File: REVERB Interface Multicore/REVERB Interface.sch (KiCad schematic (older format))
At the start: 71 parts, among them J1 RPiZeroW, J2 Iridium, J3 APRS, J4 Antenna, J5 UPDI, M1 MountingHole_Pad, M2 MountingHole_Pad, M3 MountingHole_Pad, M4 MountingHole_Pad, M5 PiMount, M6 PiMount, M7 PiMount, M8 PiMount, U1 IMU, U2 MAX3232, U3 ATtiny1604-SS, U4 TXB0104D

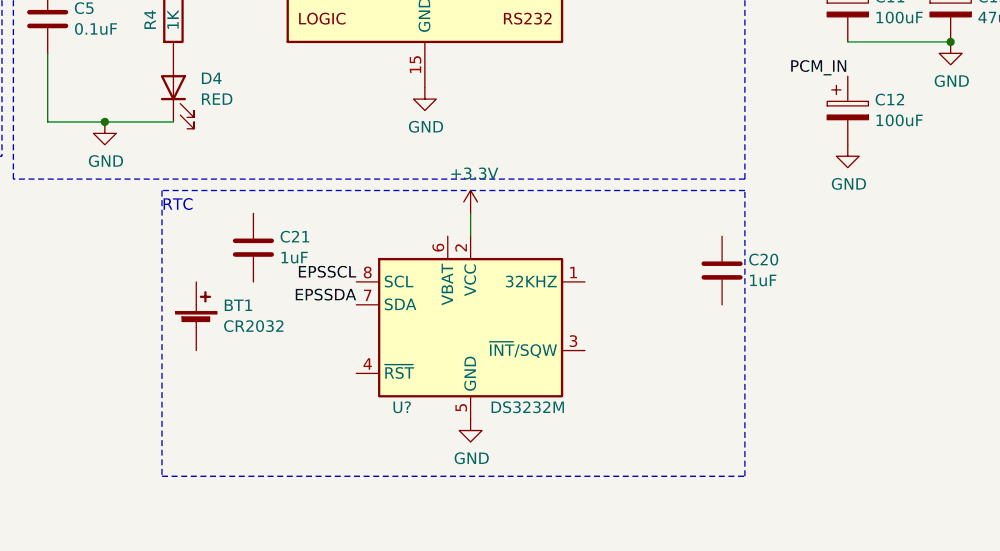
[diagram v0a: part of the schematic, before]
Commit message: add footprints, may need to use smaller battery
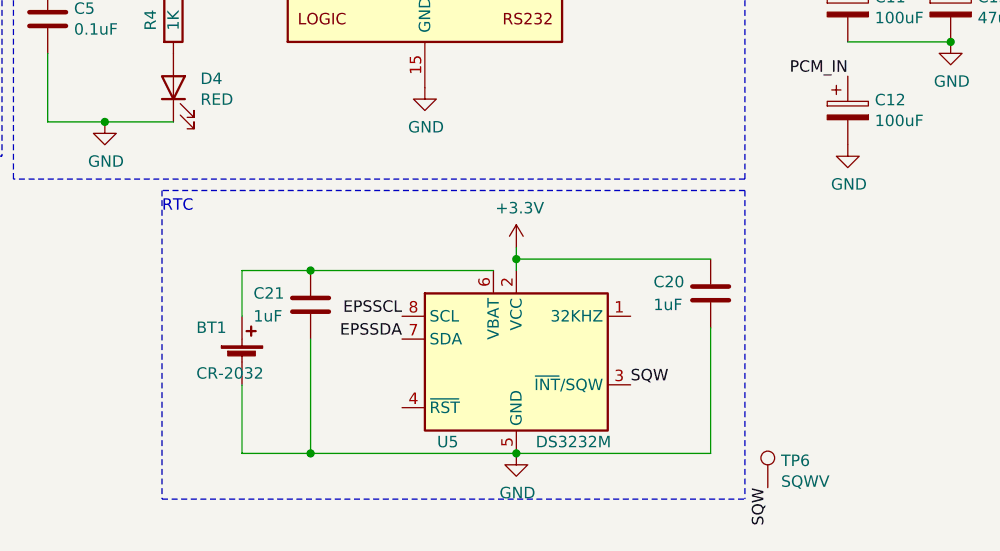
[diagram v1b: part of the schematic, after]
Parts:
- added TP6: SQWV, TestPoint:TestPoint_Pad_D2.0mm, symbol Connector:TestPoint
- BT1: value CR2032 -> CR-2032; footprint (none) -> REVERB Interface:CR2032-LINX-HLD-001-THM
- gave numbers to parts that had none: 1
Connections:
- net +3V3: now also C20.1
- net GND: now also BT1.2 (-), C20.2, C21.2
- net SQW: now reaches U5.3 (~INT~/SQW)
- net SQW: now also TP6.1
- net at U5.6 (VBAT): now also BT1.1 (+), C21.1
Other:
- moved on the sheet: BT1, C20, C21, U5
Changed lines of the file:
@@
 L Device:C C21
 U 1 1 61971DD0
-P 4750 7000
-F 0 "C21" H 4865 7046 50  0000 L CNN
-F 1 "1uF" H 4865 6955 50  0000 L CNN
-F 2 "Capacitor_SMD:C_0805_2012Metric_Pad1.18x1.45mm_HandSolder" H 4788 6850 50  0001 C CNN
-F 3 "~" H 4750 7000 50  0001 C CNN
-	1    4750 7000
+P 5000 7250
+F 0 "C21" H 4750 7300 50  0000 L CNN
+F 1 "1uF" H 4750 7200 50  0000 L CNN
+F 2 "Capacitor_SMD:C_0805_2012Metric_Pad1.18x1.45mm_HandSolder" H 5038 7100 50  0001 C CNN
+F 3 "~" H 5000 7250 50  0001 C CNN
+	1    5000 7250
 	1    0    0    -1
 $EndComp
@@
 L Device:C C20
 U 1 1 619749F1
-P 6800 7100
-F 0 "C20" H 6915 7146 50  0000 L CNN
-F 1 "1uF" H 6915 7055 50  0000 L CNN
-F 2 "Capacitor_SMD:C_0805_2012Metric_Pad1.18x1.45mm_HandSolder" H 6838 6950 50  0001 C CNN
-F 3 "~" H 6800 7100 50  0001 C CNN
-	1    6800 7100
+P 6750 7200
+F 0 "C20" H 6500 7250 50  0000 L CNN
+F 1 "1uF" H 6500 7150 50  0000 L CNN
+F 2 "Capacitor_SMD:C_0805_2012Metric_Pad1.18x1.45mm_HandSolder" H 6788 7050 50  0001 C CNN
+F 3 "~" H 6750 7200 50  0001 C CNN
+	1    6750 7200
 	1    0    0    -1
 $EndComp
-Text Label 5200 7150 2    50   ~ 0
+Text Label 5400 7300 2    50   ~ 0
 EPSSCL
-Text Label 5200 7250 2    50   ~ 0
+Text Label 5400 7400 2    50   ~ 0
 EPSSDA
 $Comp
@@
 RTC
 Wire Notes Line
-	4350 6750 4350 8000
-Wire Notes Line
-	4350 8000 6900 8000
-Wire Notes Line
-	6900 8000 6900 6750
+	4350 8100 6900 8100
 Wire Notes Line
 	6900 6750 4350 6750
 $Comp
-L power:GND #PWR?
+L power:GND #PWR0141
 U 1 1 61943473
-P 5700 7750
-F 0 "#PWR?" H 5700 7500 50  0001 C CNN
-F 1 "GND" H 5705 7577 50  0000 C CNN
-F 2 "" H 5700 7750 50  0001 C CNN
-F 3 "" H 5700 7750 50  0001 C CNN
-	1    5700 7750
+P 5900 7900
+F 0 "#PWR0141" H 5900 7650 50  0001 C CNN
+F 1 "GND" H 5905 7727 50  0000 C CNN
+F 2 "" H 5900 7900 50  0001 C CNN
+F 3 "" H 5900 7900 50  0001 C CNN
+	1    5900 7900
 	1    0    0    -1
 $EndComp
 $Comp
-L Timer_RTC:DS3232M U?
-U 1 1 61946450
-P 5700 7350
-F 0 "U?" H 5400 7000 50  0000 C CNN
-F 1 "DS3232M" H 5950 7000 50  0000 C CNN
-F 2 "Package_SO:SOIC-8_3.9x4.9mm_P1.27mm" H 5750 6850 50  0001 C CNN
-F 3 "http://datasheets.maximintegrated.com/en/ds/DS3232M.pdf" H 5970 7500 50  0001 C CNN
-	1    5700 7350
+L power:+3.3V #PWR0142
+U 1 1 61947E10
+P 5900 7000
+F 0 "#PWR0142" H 5900 6850 50  0001 C CNN
+F 1 "+3.3V" H 5915 7173 50  0000 C CNN
+F 2 "" H 5900 7000 50  0001 C CNN
+F 3 "" H 5900 7000 50  0001 C CNN
+	1    5900 7000
+	1    0    0    -1
+$EndComp
+Wire Wire Line
+	5900 7000 5900 7050
+Wire Wire Line
+	5800 7100 5000 7100
+Wire Wire Line
+	4700 7100 4700 7300
+Connection ~ 5000 7100
+Wire Wire Line
+	5000 7100 4700 7100
+Wire Wire Line
+	4700 7600 4700 7900
+Wire Wire Line
+	4700 7900 5000 7900
+Connection ~ 5900 7900
+Connection ~ 5000 7900
+Wire Wire Line
+	5000 7900 5900 7900
+Wire Wire Line
+	5000 7400 5000 7900
+Wire Wire Line
+	6750 7050 5900 7050
+Connection ~ 5900 7050
+Wire Wire Line
+	5900 7050 5900 7100
+Wire Wire Line
+	5900 7900 6750 7900
+Wire Wire Line
+	6750 7900 6750 7350
+Text Label 6400 7600 0    50   ~ 0
+SQW
+$Comp
+L Connector:TestPoint TP6
+U 1 1 61969E5D
+P 7000 8050
+F 0 "TP6" H 7058 8168 50  0000 L CNN
+F 1 "SQWV" H 7058 8077 50  0000 L CNN
+F 2 "TestPoint:TestPoint_Pad_D2.0mm" H 7200 8050 50  0001 C CNN
+F 3 "~" H 7200 8050 50  0001 C CNN
+	1    7000 8050
+	1    0    0    -1
+$EndComp
+Text Label 7000 8050 3    50   ~ 0
+SQW
+Wire Notes Line
+	4350 6750 4350 8100
+Wire Notes Line
+	6900 6750 6900 8100
+$Comp
+L Device:Battery_Cell BT1
+U 1 1 6194D163
+P 4700 7500
+F 0 "BT1" H 4500 7650 50  0000 L CNN
+F 1 "CR-2032" H 4500 7450 50  0000 L CNN
+F 2 "REVERB Interface:CR2032-LINX-HLD-001-THM" V 4700 7560 50  0001 C CNN
+F 3 "~" V 4700 7560 50  0001 C CNN
+	1    4700 7500
 	1    0    0    -1
 $EndComp
 $Comp
-L power:+3.3V #PWR?
-U 1 1 61947E10
-P 5700 6850
-F 0 "#PWR?" H 5700 6700 50  0001 C CNN
-F 1 "+3.3V" H 5715 7023 50  0000 C CNN
-F 2 "" H 5700 6850 50  0001 C CNN
-F 3 "" H 5700 6850 50  0001 C CNN
-	1    5700 6850
+L Timer_RTC:DS3232M U5
+U 1 1 61946450
+P 5900 7500
+F 0 "U5" H 5600 7150 50  0000 C CNN
+F 1 "DS3232M" H 6150 7150 50  0000 C CNN
+F 2 "Package_SO:SOIC-8_3.9x4.9mm_P1.27mm" H 5950 7000 50  0001 C CNN
+F 3 "http://datasheets.maximintegrated.com/en/ds/DS3232M.pdf" H 6170 7650 50  0001 C CNN
+	1    5900 7500
 	1    0    0    -1
 $EndComp
-Wire Wire Line
-	5700 6850 5700 6950
-$Comp
-L Device:Battery_Cell BT1
-U 1 1 6194D163
-P 4500 7350
-F 0 "BT1" H 4618 7446 50  0000 L CNN
-F 1 "CR2032" H 4618 7355 50  0000 L CNN
-F 2 "" V 4500 7410 50  0001 C CNN
-F 3 "~" V 4500 7410 50  0001 C CNN
-	1    4500 7350
-	1    0    0    -1
-$EndComp

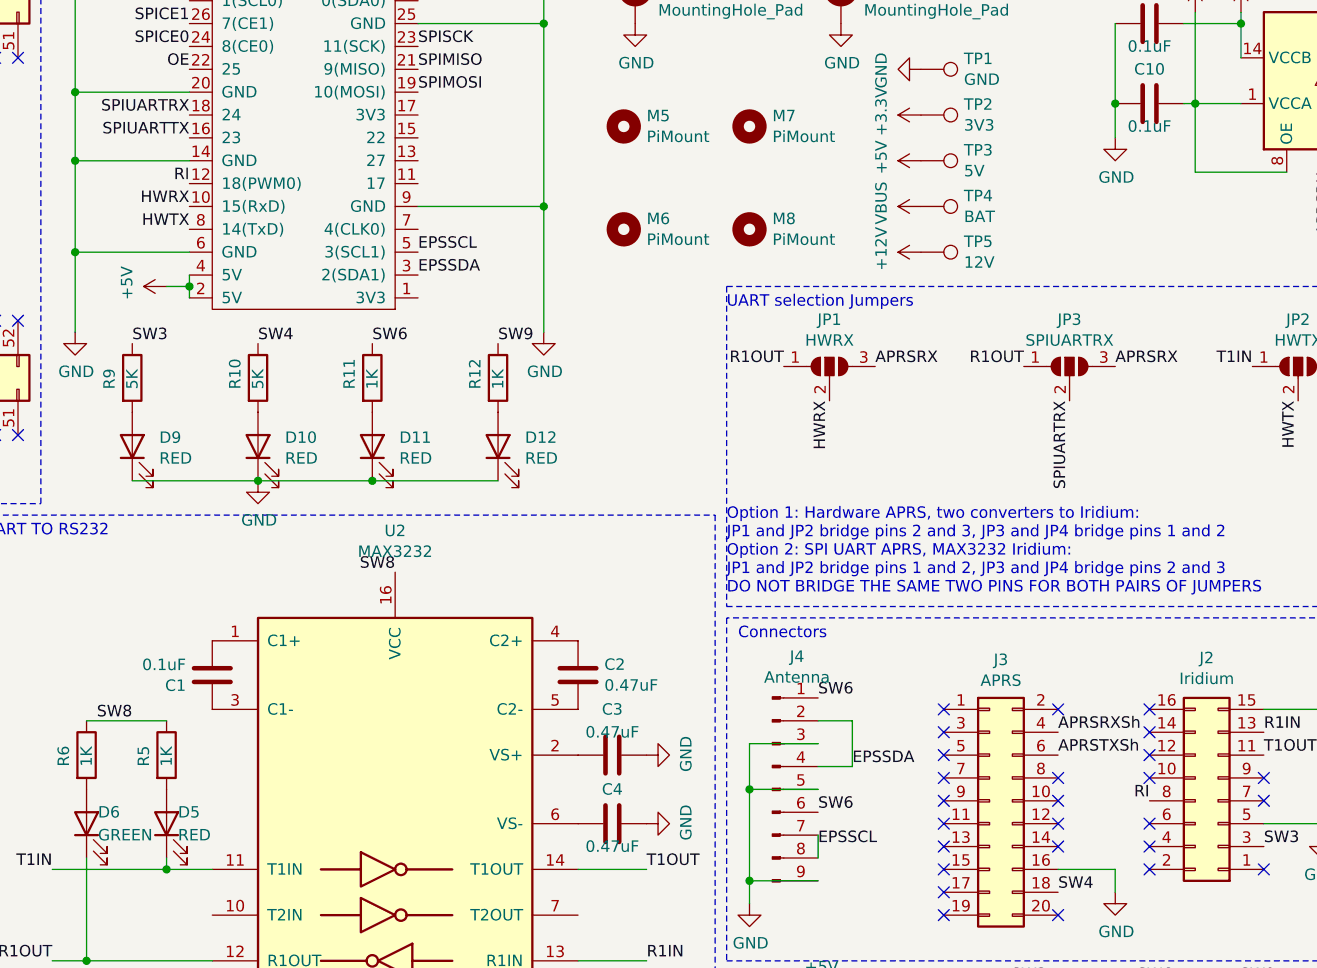
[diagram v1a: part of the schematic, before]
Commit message: Remove RI line
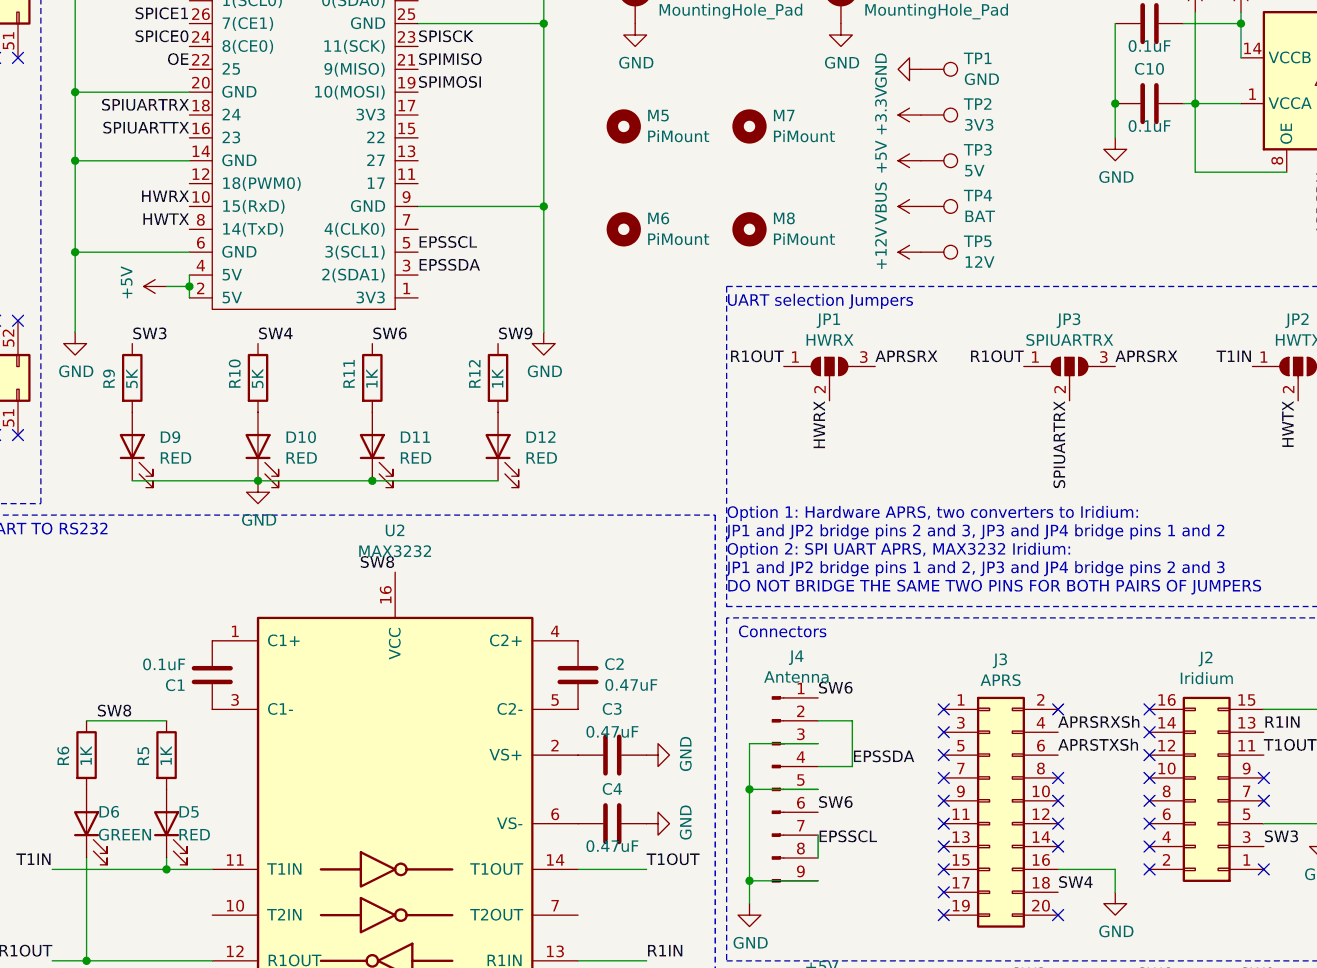
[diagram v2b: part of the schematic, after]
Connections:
- net RI: no longer names the net of J1.12 (18(PWM0))
- net RI: no longer J2.8 (Pin_8)
- no-connect marks 97 -> 98
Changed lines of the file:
@@
 	9550 4500 9300 4500
 Connection ~ 9550 5000
-Text Label 8800 4900 2    50   ~ 0
-RI
-Text Label 4600 2200 2    50   ~ 0
-RI
 $Comp
 L Device:C C21
@@
 	1    0    0    -1
 $EndComp
+NoConn ~ 8800 4900
 $EndSCHEMATC

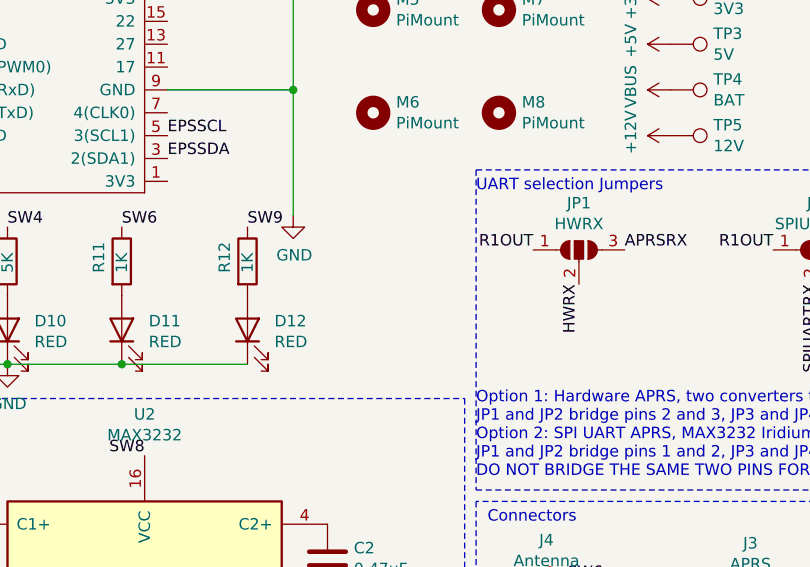
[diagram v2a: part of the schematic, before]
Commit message: add usb switch
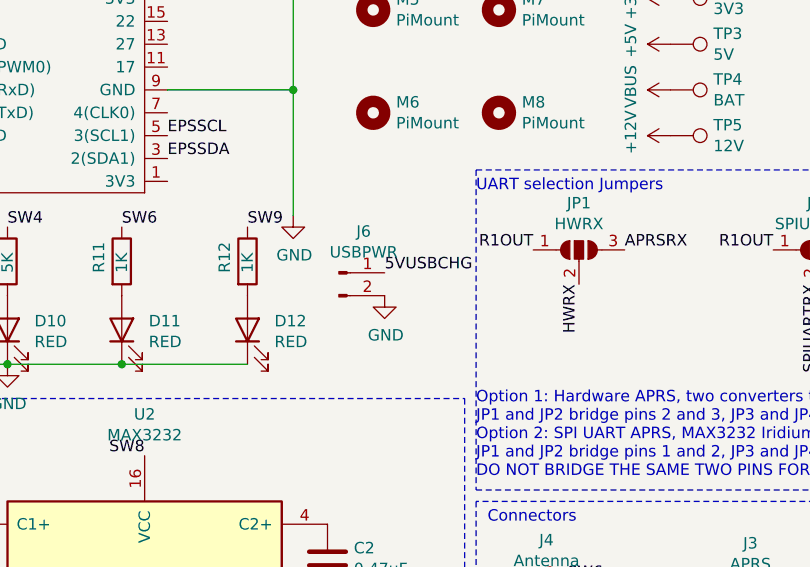
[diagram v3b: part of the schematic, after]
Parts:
- added J6: USBPWR, Connector_JST:JST_XH_B2B-XH-A_1x02_P2.50mm_Vertical, symbol Connector:Conn_01x02_Male
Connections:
- net 5VUSBCHG: now also J6.1 (Pin_1)
- net GND: now also J6.2 (Pin_2)
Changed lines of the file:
@@
 $EndComp
 NoConn ~ 8800 4900
+$Comp
+L Connector:Conn_01x02_Male J6
+U 1 1 61975C7D
+P 6350 3100
+F 0 "J6" H 6458 3281 50  0000 C CNN
+F 1 "USBPWR" H 6458 3190 50  0000 C CNN
+F 2 "Connector_JST:JST_XH_B2B-XH-A_1x02_P2.50mm_Vertical" H 6350 3100 50  0001 C CNN
+F 3 "~" H 6350 3100 50  0001 C CNN
+	1    6350 3100
+	1    0    0    -1
+$EndComp
+Text Label 6550 3100 0    50   ~ 0
+5VUSBCHG
+$Comp
+L power:GND #PWR0143
+U 1 1 6198130C
+P 6550 3200
+F 0 "#PWR0143" H 6550 2950 50  0001 C CNN
+F 1 "GND" H 6555 3027 50  0000 C CNN
+F 2 "" H 6550 3200 50  0001 C CNN
+F 3 "" H 6550 3200 50  0001 C CNN
+	1    6550 3200
+	1    0    0    -1
+$EndComp
 $EndSCHEMATC

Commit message: Move some parts around, remove UART LEDs, .step export, push v1.6
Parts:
- removed D1, D5: RED, LED_SMD:LED_0805_2012Metric_Pad1.15x1.40mm_HandSolder, symbol Device:LED
- removed D2, D6: GREEN, LED_SMD:LED_0805_2012Metric_Pad1.15x1.40mm_HandSolder, symbol Device:LED
- removed R1, R2, R5, R6: 1K, Resistor_SMD:R_0805_2012Metric_Pad1.20x1.40mm_HandSolder, symbol Device:R
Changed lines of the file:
@@
 Title "TJ REVERB Interface Board"
 Date "2021-10-03"
-Rev "1.5"
+Rev "1.6"
 Comp "TJ Nanosat Club"
 Comment1 "Redesign from previous Eagle designs"
@@
 SPICE0
 $Comp
-L Device:LED D2
-U 1 1 61681979
-P 1150 5700
-F 0 "D2" V 1200 5850 50  0000 R CNN
-F 1 "GREEN" V 1100 6000 50  0000 R CNN
-F 2 "LED_SMD:LED_0805_2012Metric_Pad1.15x1.40mm_HandSolder" H 1150 5700 50  0001 C CNN
-F 3 "~" H 1150 5700 50  0001 C CNN
-	1    1150 5700
-	0    -1   -1   0
-$EndComp
-$Comp
-L Device:R R2
-U 1 1 6168462F
-P 1150 5400
-F 0 "R2" V 1050 5350 50  0000 L CNN
-F 1 "1K" V 1150 5350 50  0000 L CNN
-F 2 "Resistor_SMD:R_0805_2012Metric_Pad1.20x1.40mm_HandSolder" V 1080 5400 50  0001 C CNN
-F 3 "~" H 1150 5400 50  0001 C CNN
-	1    1150 5400
-	1    0    0    -1
-$EndComp
-$Comp
 L Device:LED D3
 U 1 1 6169D0A8
@@
 Wire Wire Line
 	3850 5850 4400 5850
-$Comp
-L Device:LED D5
-U 1 1 616CB109
-P 4500 5000
-F 0 "D5" V 4550 4950 50  0000 R CNN
-F 1 "RED" V 4450 4950 50  0000 R CNN
-F 2 "LED_SMD:LED_0805_2012Metric_Pad1.15x1.40mm_HandSolder" H 4500 5000 50  0001 C CNN
-F 3 "~" H 4500 5000 50  0001 C CNN
-	1    4500 5000
-	0    -1   -1   0
-$EndComp
-$Comp
-L Device:R R5
-U 1 1 616CB10F
-P 4500 4700
-F 0 "R5" V 4400 4650 50  0000 L CNN
-F 1 "1K" V 4500 4650 50  0000 L CNN
-F 2 "Resistor_SMD:R_0805_2012Metric_Pad1.20x1.40mm_HandSolder" V 4430 4700 50  0001 C CNN
-F 3 "~" H 4500 4700 50  0001 C CNN
-	1    4500 4700
-	1    0    0    -1
-$EndComp
-$Comp
-L Device:R R6
-U 1 1 616D0A78
-P 4150 4700
-F 0 "R6" V 4050 4650 50  0000 L CNN
-F 1 "1K" V 4150 4650 50  0000 L CNN
-F 2 "Resistor_SMD:R_0805_2012Metric_Pad1.20x1.40mm_HandSolder" V 4080 4700 50  0001 C CNN
-F 3 "~" H 4150 4700 50  0001 C CNN
-	1    4150 4700
-	1    0    0    -1
-$EndComp
-Text Label 4350 4550 2    50   ~ 0
-SW8
-$Comp
-L Device:LED D6
-U 1 1 616D0A72
-P 4150 5000
-F 0 "D6" V 4200 4950 50  0000 R CNN
-F 1 "GREEN" V 4100 4950 50  0000 R CNN
-F 2 "LED_SMD:LED_0805_2012Metric_Pad1.15x1.40mm_HandSolder" H 4150 5000 50  0001 C CNN
-F 3 "~" H 4150 5000 50  0001 C CNN
-	1    4150 5000
-	0    -1   -1   0
-$EndComp
-Wire Wire Line
-	4700 5200 4500 5200
-Wire Wire Line
-	4000 5600 4150 5600
-Wire Wire Line
-	4150 4550 4500 4550
 Wire Wire Line
 	6300 5200 6600 5200
 Wire Wire Line
 	6300 5600 6600 5600
-Wire Wire Line
-	4500 5150 4500 5200
-Connection ~ 4500 5200
-Wire Wire Line
-	4500 5200 4000 5200
-Wire Wire Line
-	4150 5150 4150 5600
-Connection ~ 4150 5600
-Wire Wire Line
-	4150 5600 4700 5600
 Text Notes 500  3750 0    50   ~ 0
 Secondary uC
@@
 Text Label 3100 5150 0    50   ~ 0
 SPICE0
-Text Label 1150 5850 3    50   ~ 0
-SPIUARTRX
 Wire Notes Line
 	500  3650 3650 3650
@@
 	1    0    0    -1
 $EndComp
-$Comp
-L Device:R R1
-U 1 1 61683EE4
-P 1500 5400
-F 0 "R1" V 1400 5350 50  0000 L CNN
-F 1 "1K" V 1500 5350 50  0000 L CNN
-F 2 "Resistor_SMD:R_0805_2012Metric_Pad1.20x1.40mm_HandSolder" V 1430 5400 50  0001 C CNN
-F 3 "~" H 1500 5400 50  0001 C CNN
-	1    1500 5400
-	1    0    0    -1
-$EndComp
-$Comp
-L Device:LED D1
-U 1 1 61680797
-P 1500 5700
-F 0 "D1" V 1550 5650 50  0000 R CNN
-F 1 "RED" V 1450 5650 50  0000 R CNN
-F 2 "LED_SMD:LED_0805_2012Metric_Pad1.15x1.40mm_HandSolder" H 1500 5700 50  0001 C CNN
-F 3 "~" H 1500 5700 50  0001 C CNN
-	1    1500 5700
-	0    -1   -1   0
-$EndComp
-Text Label 1500 5850 3    50   ~ 0
-SPIUARTTX
-Wire Wire Line
-	1150 5250 1500 5250
-Text Label 1250 5250 0    50   ~ 0
-SW10
 Text Label 3100 4750 0    50   ~ 0
 SLVRST
@@
 	1    0    0    -1
 $EndComp
+Wire Wire Line
+	4000 5200 4700 5200
+Wire Wire Line
+	4000 5600 4700 5600
 $EndSCHEMATC
